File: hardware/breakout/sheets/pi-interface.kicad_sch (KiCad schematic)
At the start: 18 parts, among them J10 Barcode spare 1, J11 Barcode spare 2, J12 Barcode spare 3, J13 Eye camera trigger out (BNC), J14 Behavior camera trigger out 1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, J15 Behavior camera trigger out 2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, J16 Behavior camera trigger out 3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, J17 Behavior camera trigger out 4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, J18 Internal USB-A (sync-module p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, J7 Sync-module 40-pin GPIO heade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, J8 Barcode -> NI optocoupler (Ta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, J9 Barcode -> Intan optocoupler 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, U14 SN74LVC541APW, U15 SN74AHCT541PW

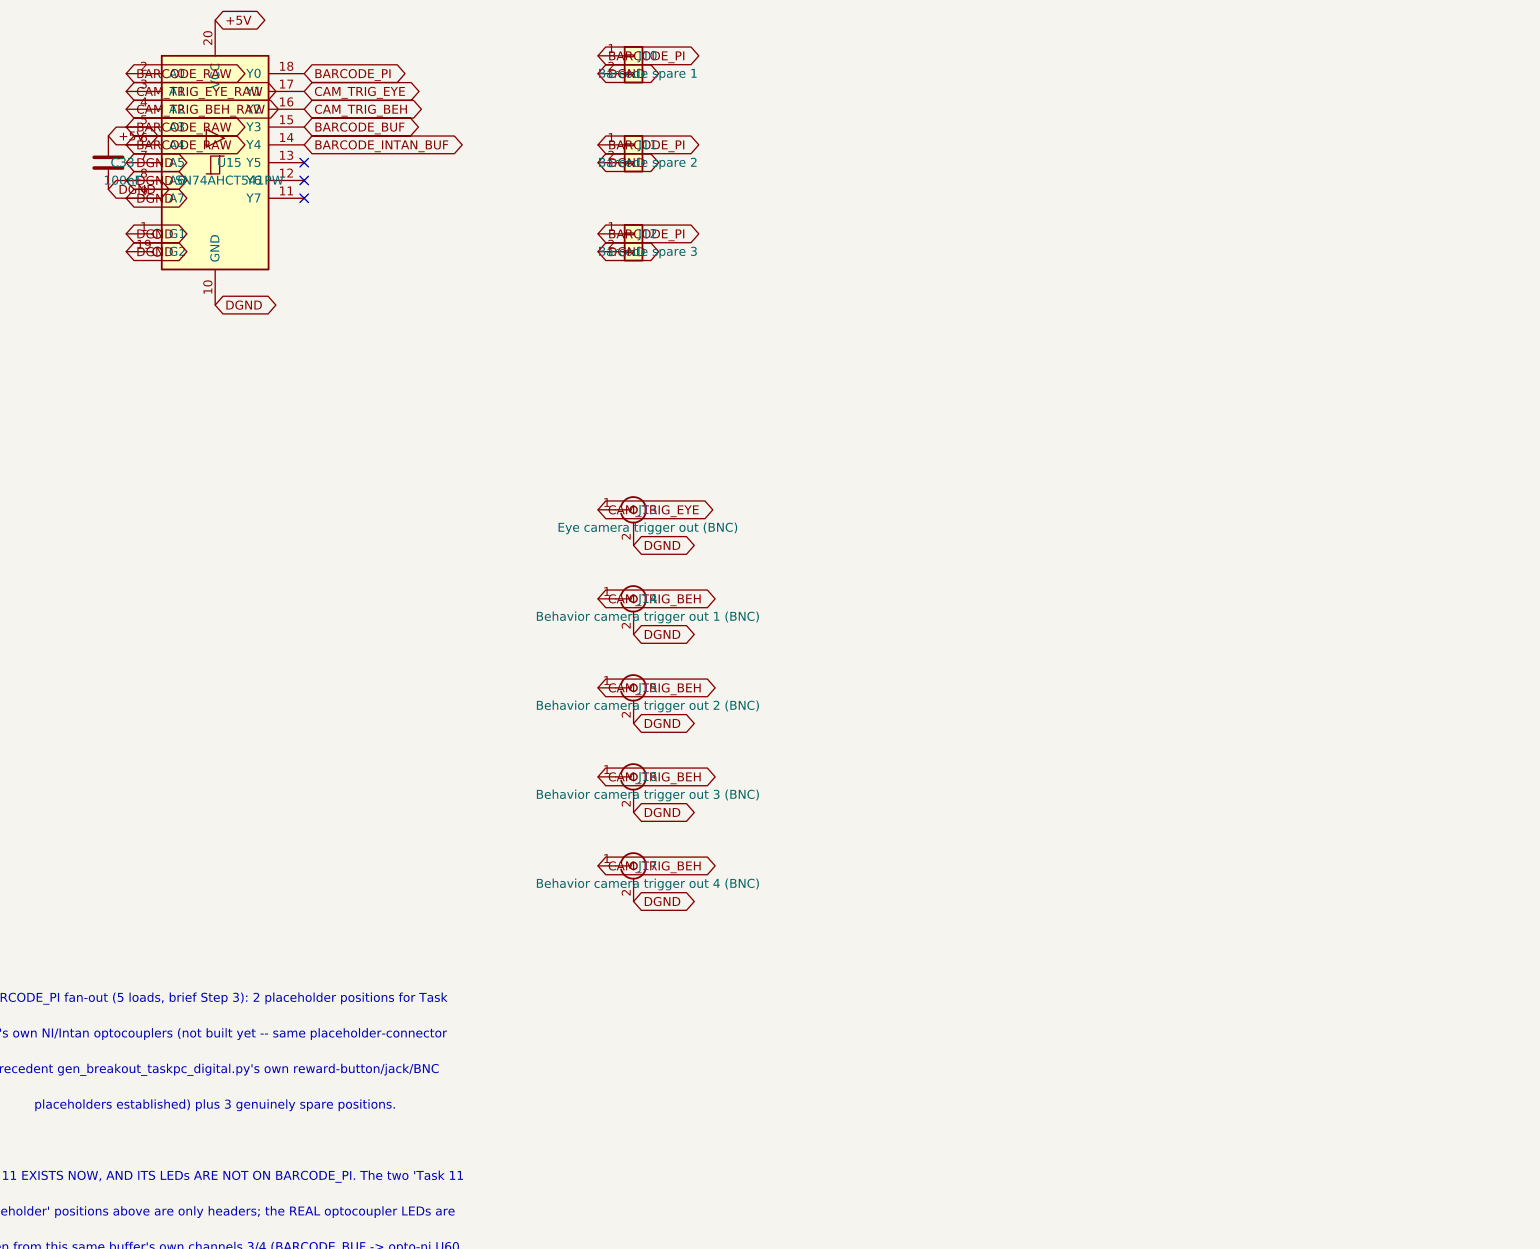
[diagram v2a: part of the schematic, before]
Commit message: feat(breakout): chassis earth stud, power-good LEDs, rail test points, main fusing
Change D: five things a rack instrument needs that this board lacked
(spec Sec.9.8), four landing on power.kicad_sch and one on
pi-interface.kicad_sch:

- Chassis earth stud (J56): an M3 mounting hole with a connected pad --
  the mounting point spec Sec.5.6's cage-to-rack bond can land on. Carries
  a new CHASSIS_GND net, joined to DGND at exactly one net tie (NT3),
  mirroring the fan return's own NT2 treatment.
- Power-good LED per rail (D40/D41/D42, +12V/-12V/+5V): a failed rail is
  otherwise invisible until the data is wrong. ~4.5mA each, negligible
  against any rail's own budget.
- Rail test points (TP1-TP7): one per voltage rail plus one on INTAN_GND --
  the isolated domain's own reference, without which ISO_P12/ISO_N12
  cannot actually be measured (INTAN_GND is galvanically separate from
  AGND/DGND).
- Main input fusing (F2/F3/F4, +-12V/+5V): the fans already had a
  polyfuse; the main rails did not. Same real part as the fan feed's own
  F1 (Littelfuse 1206L050/15YR). A higher-current Bourns MF-SM alternative
  was evaluated and rejected: its own datasheet advises against hand
  soldering, which would add a third accepted hand-solderability exception
  beyond the two this board already documents. +-12V's own real total draw
  is flagged for bench confirmation rather than presented as fully closed.
- Barcode heartbeat LED (D43, on pi-interface.kicad_sch): a third
  dedicated leg off the trigger buffer's own BARCODE_RAW input, so the
  visible "sync box alive" LED never loads the real barcode net.

Extended check_breakout_power_netlist.py and
check_breakout_pi_interface_netlist.py with topology checks for every new
item, each with a genuinely-firing negative control, and wired in the
shared row-pitch collision guard where it was missing.

Regenerated hardware/breakout/netlist-contract.json and both BOM CSVs
(raw + order, +14 rows) against this cumulative state; updated
pro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
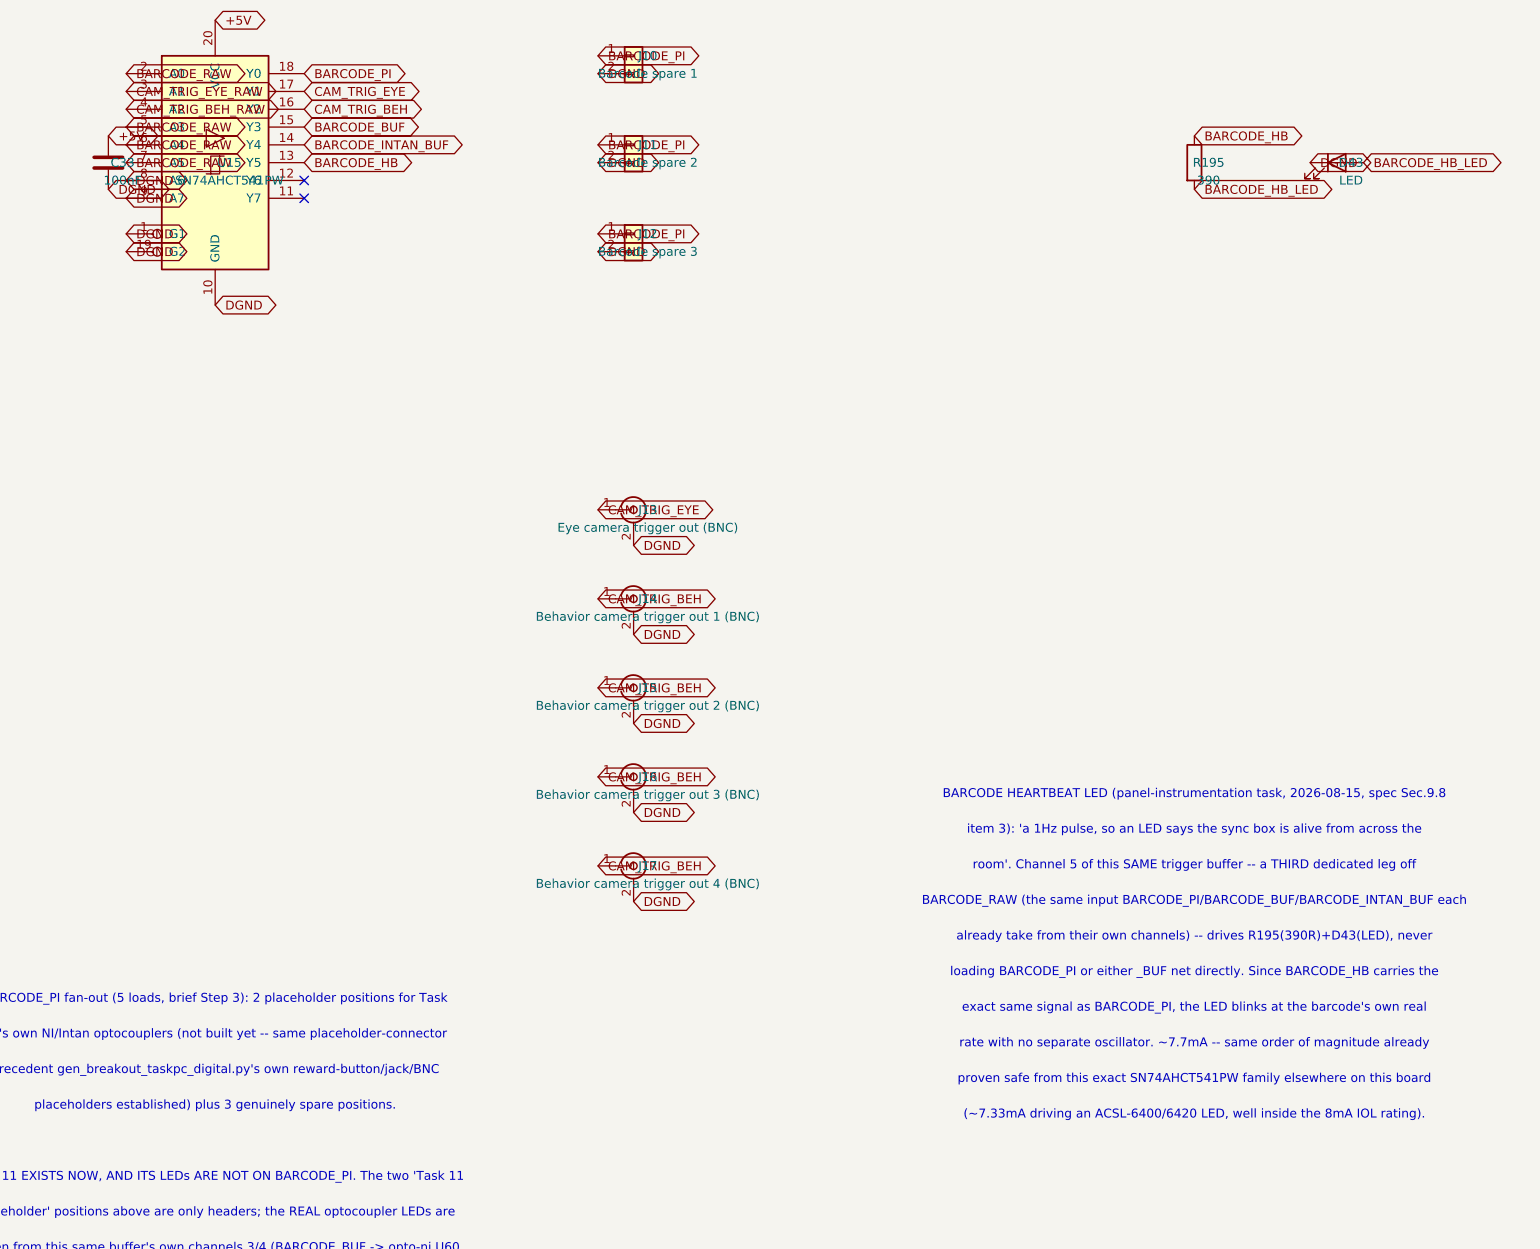
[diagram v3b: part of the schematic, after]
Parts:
- added D43: LED, LED_SMD:LED_0603_1608Metric_Pad1.05x0.95mm_HandSolder, symbol Device:LED
- added R195: 390, Resistor_SMD:R_0603_1608Metric, symbol Device:R
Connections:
- net BARCODE_RAW: now also U15.7 (A5)
- net DGND: now also D43.1 (K); no longer U15.7 (A5)
- net BARCODE_HB: now reaches U15.13 (Y5)
- net BARCODE_HB: now also R195.1
- new net BARCODE_HB_LED: D43.2 (A), R195.2
- no-connect marks 16 -> 15
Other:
- note added: "(~7.33mA driving an ACSL-6400/6420 LED, well inside the 8mA IOL rating)."
- note added: "BARCODE HEARTBEAT LED (panel-instrumentation task, 2026-08-15, spec Sec.9.8"
- note added: "BARCODE_RAW (the same input BARCODE_PI/BARCODE_BUF/BARCODE_INTAN_BUF each"
- note added: "already take from their own channels) -- drives R195(390R)+D43(LED), never"
- note added: "exact same signal as BARCODE_PI, the LED blinks at the barcode's own real"
- note added: "item 3): 'a 1Hz pulse, so an LED says the sync box is alive from across the"
- note added: "loading BARCODE_PI or either _BUF net directly. Since BARCODE_HB carries the"
- note added: "proven safe from this exact SN74AHCT541PW family elsewhere on this board"
- note added: "rate with no separate oscillator. ~7.7mA -- same order of magnitude already"
- note added: "room'. Channel 5 of this SAME trigger buffer -- a THIRD dedicated leg off"

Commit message: fix(hardware): drive the optocoupler LEDs (F1, both halves)
430R never switched these LEDs. The original sizing solved
(5.0 - V_OL - V_F)/I correctly but against the rail's NOMINAL 5.00V and
V_F TYP; +5V reaches the anodes through F4 and D3 (0.42-0.49V of drop)
and V_F's worst case is 1.80V, so the real worst-case current was ~5mA
against the ACSL-6xx0's 7.0mA I_FH minimum. 30 channels were not
guaranteed to switch for seventy-three commits.

Both halves land together because neither is shippable alone -- 430R
starves the LED, and 249R (~12.7mA) overloads a single 7.5mA output.

Resistors, rail-aware: 430R -> 249R on the 30 LEDs fed from +5V, ->
301R on the 2 fed from ISO_5V. ISO_5V is regulated locally with nothing
in series, so 249R there would give 15.1mA -- past the 15mA ABSOLUTE
maximum. One value is wrong on one rail or the other.

Paralleling: every buffer-driven LED now has two SN74AHCT541 outputs
from tied inputs. Four new packages (U70-U73) plus C151-C154, 5 buffer
packages to 9, 6 spare channels. Channel maps are mirrored from the
tables that built the first leg rather than re-listed, so the legs
cannot drift apart. Refdes minted out of band, above the board maximum:
8 refs added, 0 removed, 0 renumbered.

This also fixes a per-PACKAGE limit no per-pin check could see. The
AHCT541's GND absolute maximum is 75mA (SCLS269Q 4.1, not the 100mA
hardware/README.md claimed); U8/U9 drive eight LEDs each; the drive is
active-low and the event bus idles at 0x0000, so sixteen LEDs are lit
CONTINUOUSLY. At 249R unparalleled that is ~101mA through one ground
pin. Paralleled it is 55.6mA worst case.

RHS_STIM_OUT's LED moves to a new buffered leg (RHS_STIM_OUT_BUF, off
U11's last two spare channels). It was the one channel driven by an
ACSL-6420 output rather than a buffer -- a deliberate, checked exception
that was correct at 430R (8.61mA of a 13mA budget) and not correct at
249R (13.85mA with its pull-up). The exception did not change; the
number it had been checked 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
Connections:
- net BARCODE_BUF: now also U15.12 (Y6)
- net BARCODE_INTAN_BUF: now also U15.11 (Y7)
- net BARCODE_RAW: now also U15.8 (A6), U15.9 (A7)
- net DGND: no longer U15.8 (A6), U15.9 (A7)
- no-connect marks 15 -> 13

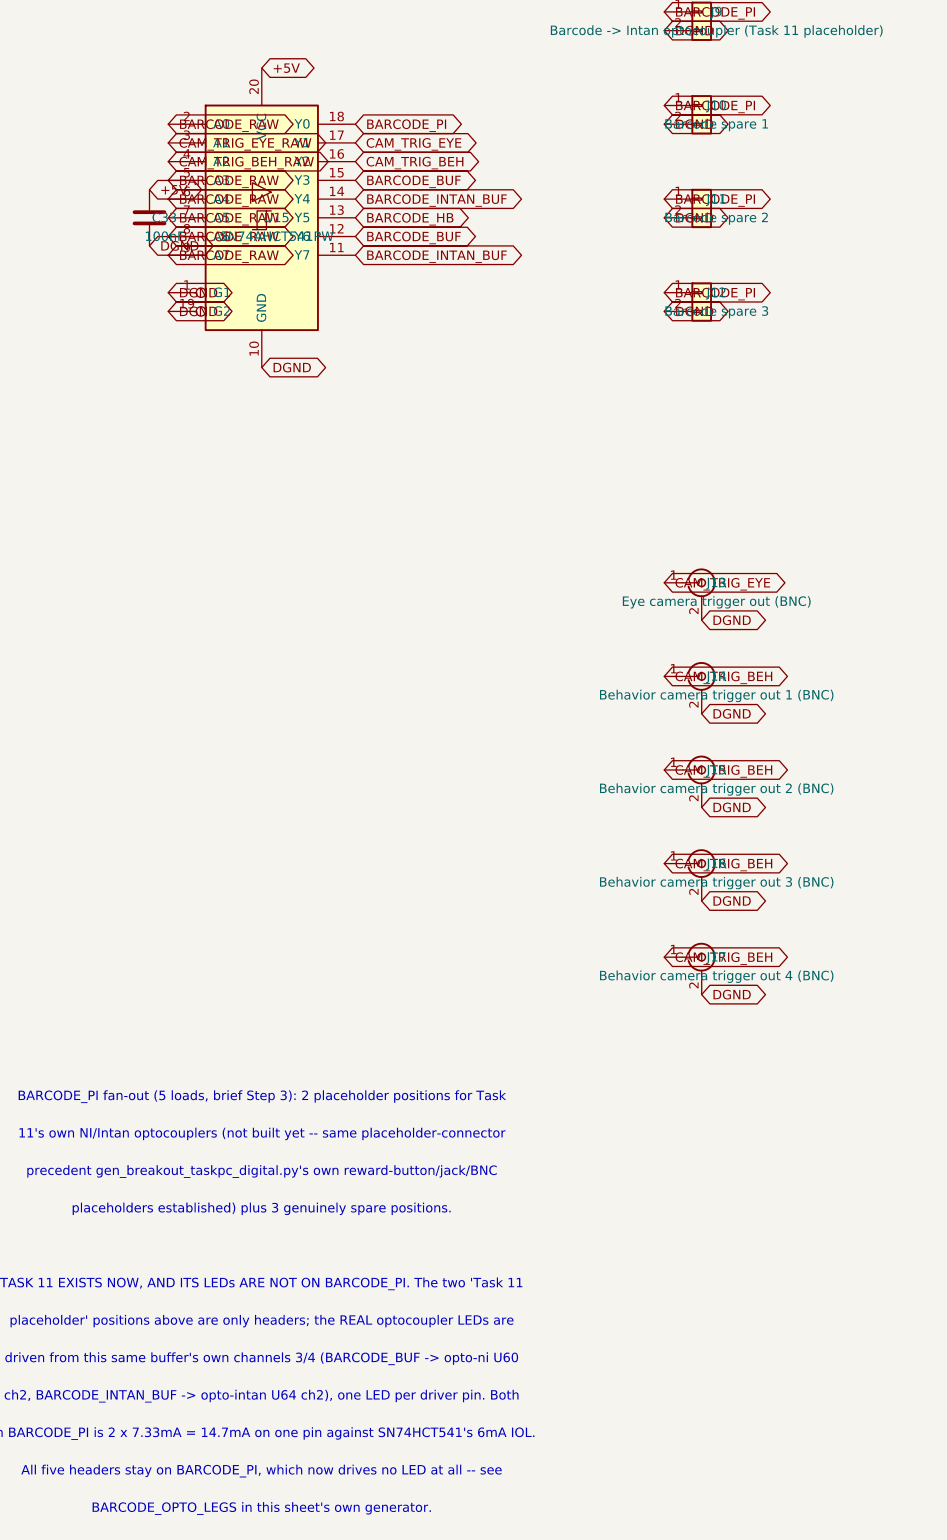
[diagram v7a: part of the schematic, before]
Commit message: fix(hardware): one driver and one series resistor per panel output (F4, M3)
F4 -- FOUR CAMERA TRIGGERS SHARED ONE UNTERMINATED OUTPUT.

CAM_TRIG_BEH drove J14-J17 from a single SN74AHCT541 output. Four parallel
coax runs present Z0/4 ~ 12.5 ohm, so the initial edge drew roughly 118 mA
against the part's 25 mA per-output ABSOLUTE maximum -- brief, but on every
edge for the life of the board. With no source termination the cameras
could also see reflections and double-trigger, which is corrupted frame
timing rather than a cosmetic fault.

Each of the five triggers now has its own buffer channel and its own 47 ohm
series resistor: CAM_TRIG_BEH splits into CAM_TRIG_BEH1..4, channel 2 of the
existing trigger buffer keeps trigger 1, and a new package (U74) takes the
other three. They still share one trigger RATE via CAM_TRIG_BEH_RAW -- spec
Sec.9.4 is unchanged -- they no longer share a driver pin.

NOT on finding F1's spare channels, which the audit expected. Those sit on
taskpc-digital, and routing an unbuffered 3.3 V trigger across the board and
its buffered copies back again is the wrong trade for a signal whose entire
problem is edge quality at the connector. Source GPIO, buffer and BNCs stay
on one sheet; the cost is one package.

47 ohm errs high on purpose. An AHCT541's own output impedance is ~25-35
ohm, so textbook series termination into 50 ohm coax would be nearer 20 ohm.
Over-damping costs a little edge rate and buys margin against the failure
that actually matters here. The first step at a high-impedance camera input
lands at ~77% of the swing before settling, far above any TTL V_IH.

M3 -- SIX BARE PANEL OUTPUTS, AND THERE WERE ELEVEN.

Series resistance added to all six the finding names: the five camera
triggers at 47 ohm, and J6 (reward driver out) at 100 ohm -- that pin's
problem is fault current from an inductive kick or a mis-plug, not
transmission-line matching, so it takes this board's established
panel-series value rather than the termination one. 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
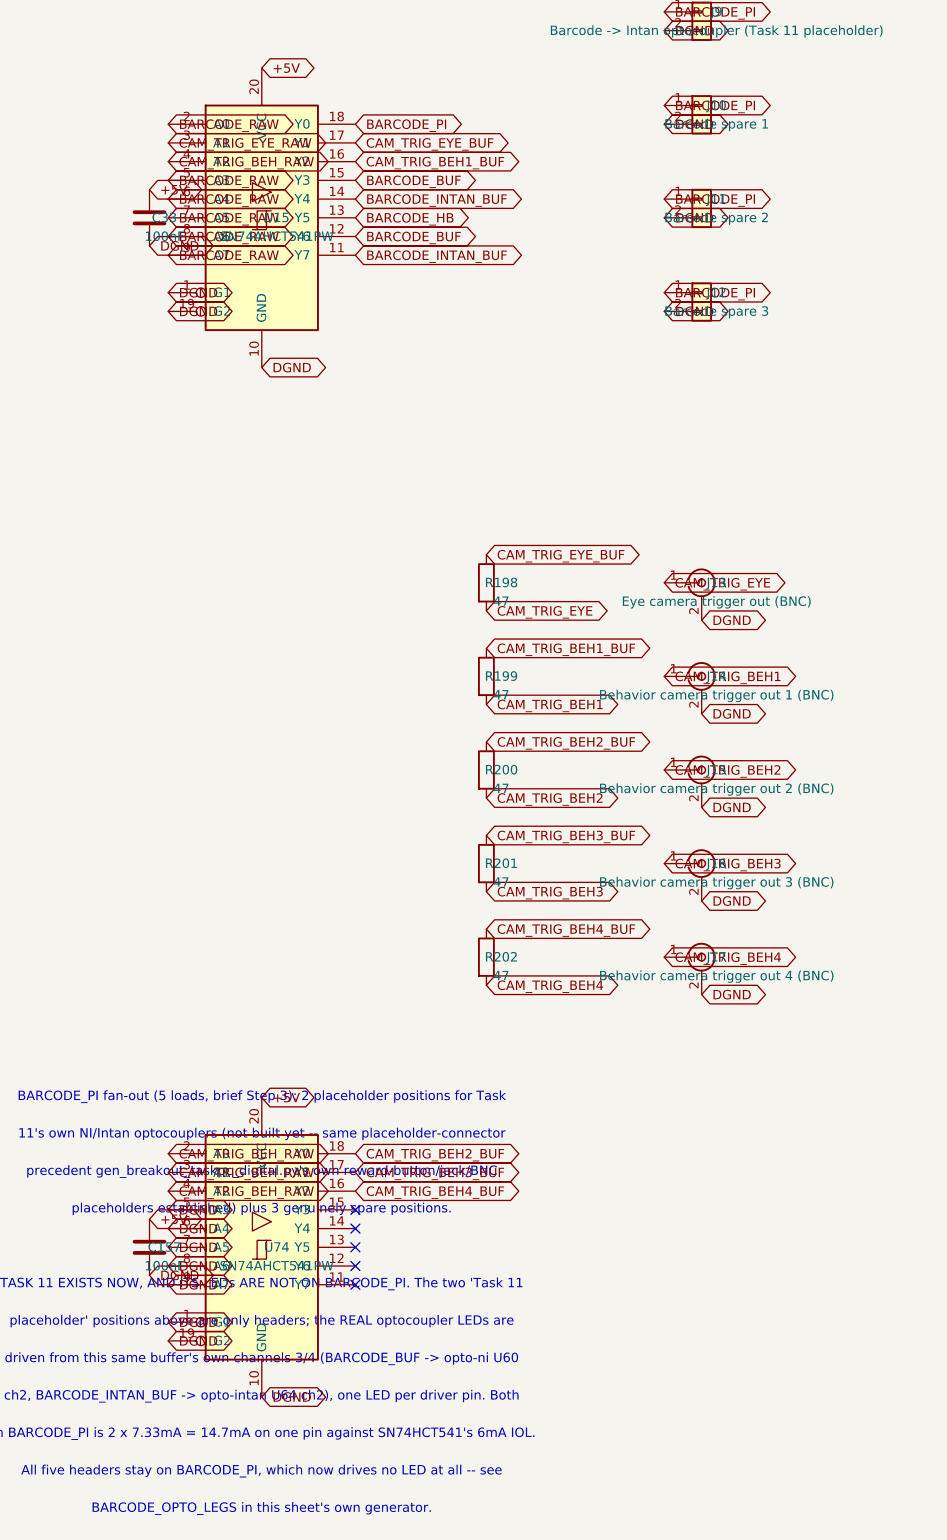
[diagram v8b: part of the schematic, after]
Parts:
- added C157: 100nF, Capacitor_SMD:C_0603_1608Metric, symbol Device:C
- added R198, R199, R200, R201, R202: 47, Resistor_SMD:R_0603_1608Metric, symbol Device:R
- added U74: SN74AHCT541PW, Package_SO:Texas_PW0020A_TSSOP-20_4.4x6.5mm_P0.65mm, symbol 74xx:74AHCT541
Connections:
- net +5V: now also C157.1, U74.20 (VCC)
- net CAM_TRIG_BEH_RAW: now also U74.2 (A0), U74.3 (A1), U74.4 (A2)
- net CAM_TRIG_EYE: now also R198.2; no longer U15.17 (Y1)
- net DGND: now also C157.2, U74.1 (G1), U74.10 (GND), U74.19 (G2), U74.5 (A3), U74.6 (A4), U74.7 (A5), U74.8 (A6), U74.9 (A7)
- removed net CAM_TRIG_BEH: J14.1 (In), J15.1 (In), J16.1 (In), J17.1 (In), U15.16 (Y2)
- new net CAM_TRIG_BEH1: J14.1 (In), R199.2
- new net CAM_TRIG_BEH1_BUF: R199.1, U15.16 (Y2)
- new net CAM_TRIG_BEH2: J15.1 (In), R200.2
- new net CAM_TRIG_BEH2_BUF: R200.1, U74.18 (Y0)
- new net CAM_TRIG_BEH3: J16.1 (In), R201.2
- new net CAM_TRIG_BEH3_BUF: R201.1, U74.17 (Y1)
- new net CAM_TRIG_BEH4: J17.1 (In), R202.2
- new net CAM_TRIG_BEH4_BUF: R202.1, U74.16 (Y2)
- new net CAM_TRIG_EYE_BUF: R198.1, U15.17 (Y1)
- no-connect marks 13 -> 18
